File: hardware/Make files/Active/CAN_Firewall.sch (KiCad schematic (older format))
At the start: 55 parts, among them CON1 BARREL_JACK, CON2 AVR-JTAG-10, CON3 AVR-AW-6, J1 +5V_SRC, J2 DB9, J3 DB9, P1 USB_OTG, P2 USB_OTG, P3 DIAG Port, SW1 SPST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

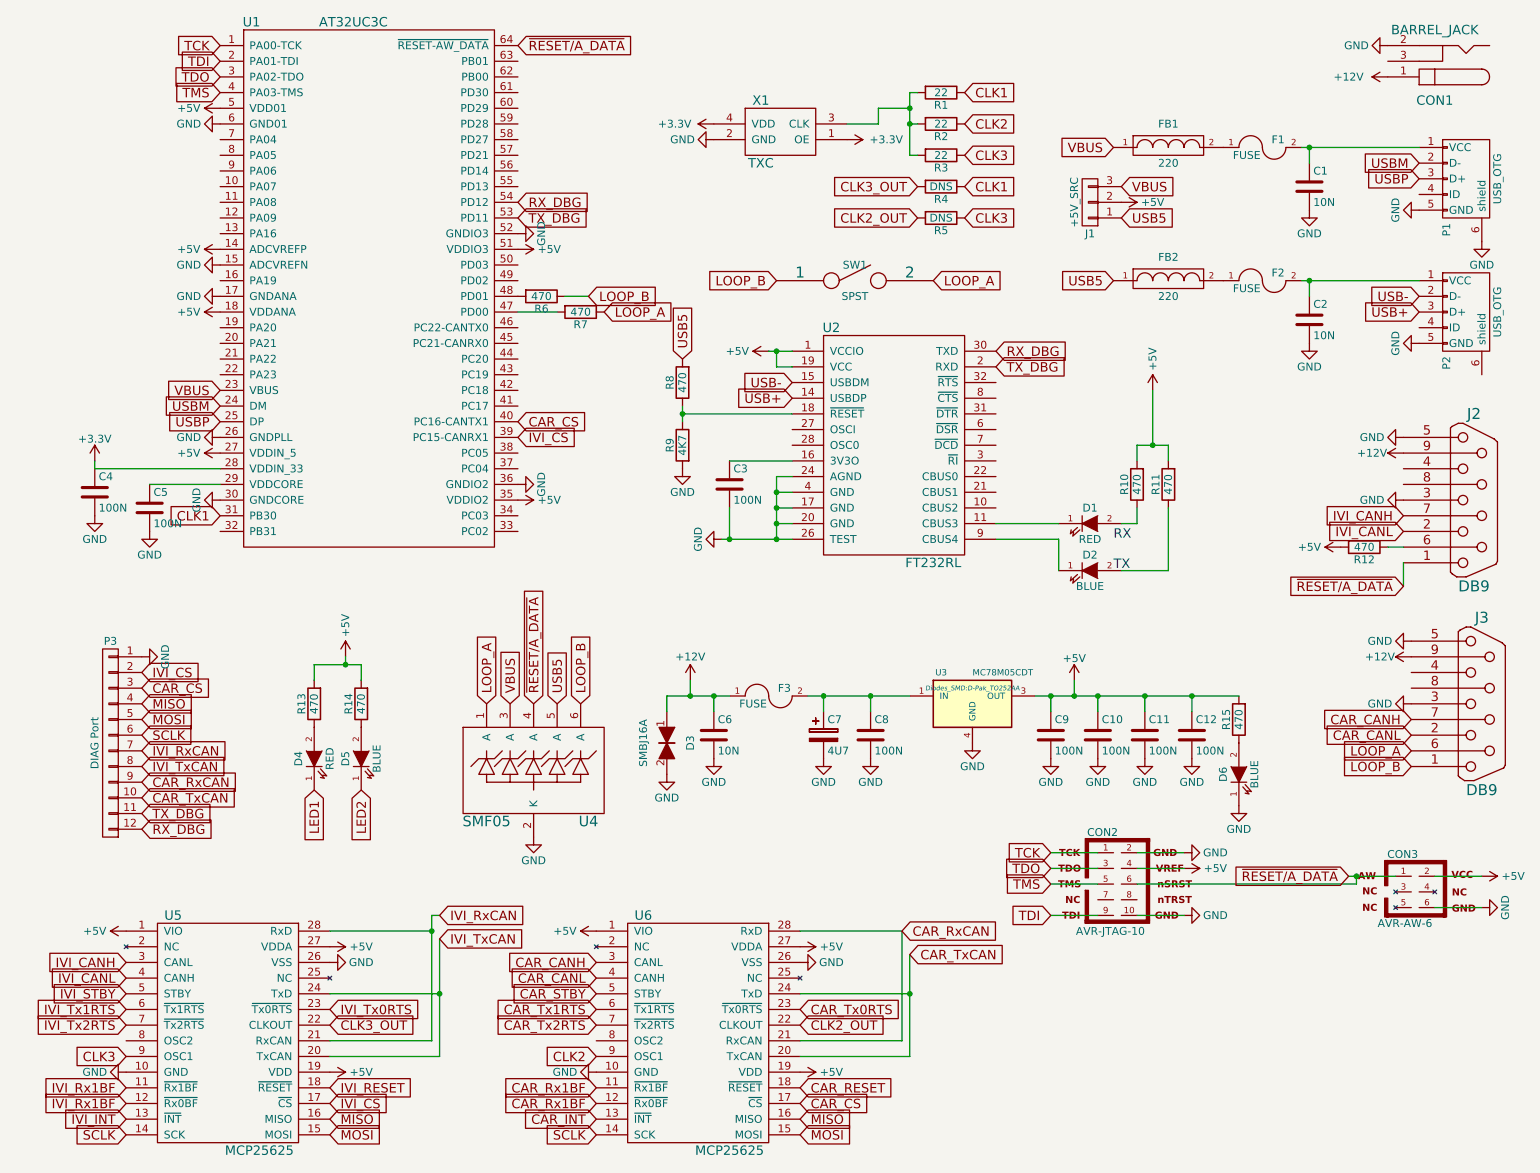
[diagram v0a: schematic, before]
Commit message: V1.1 layout pass complete
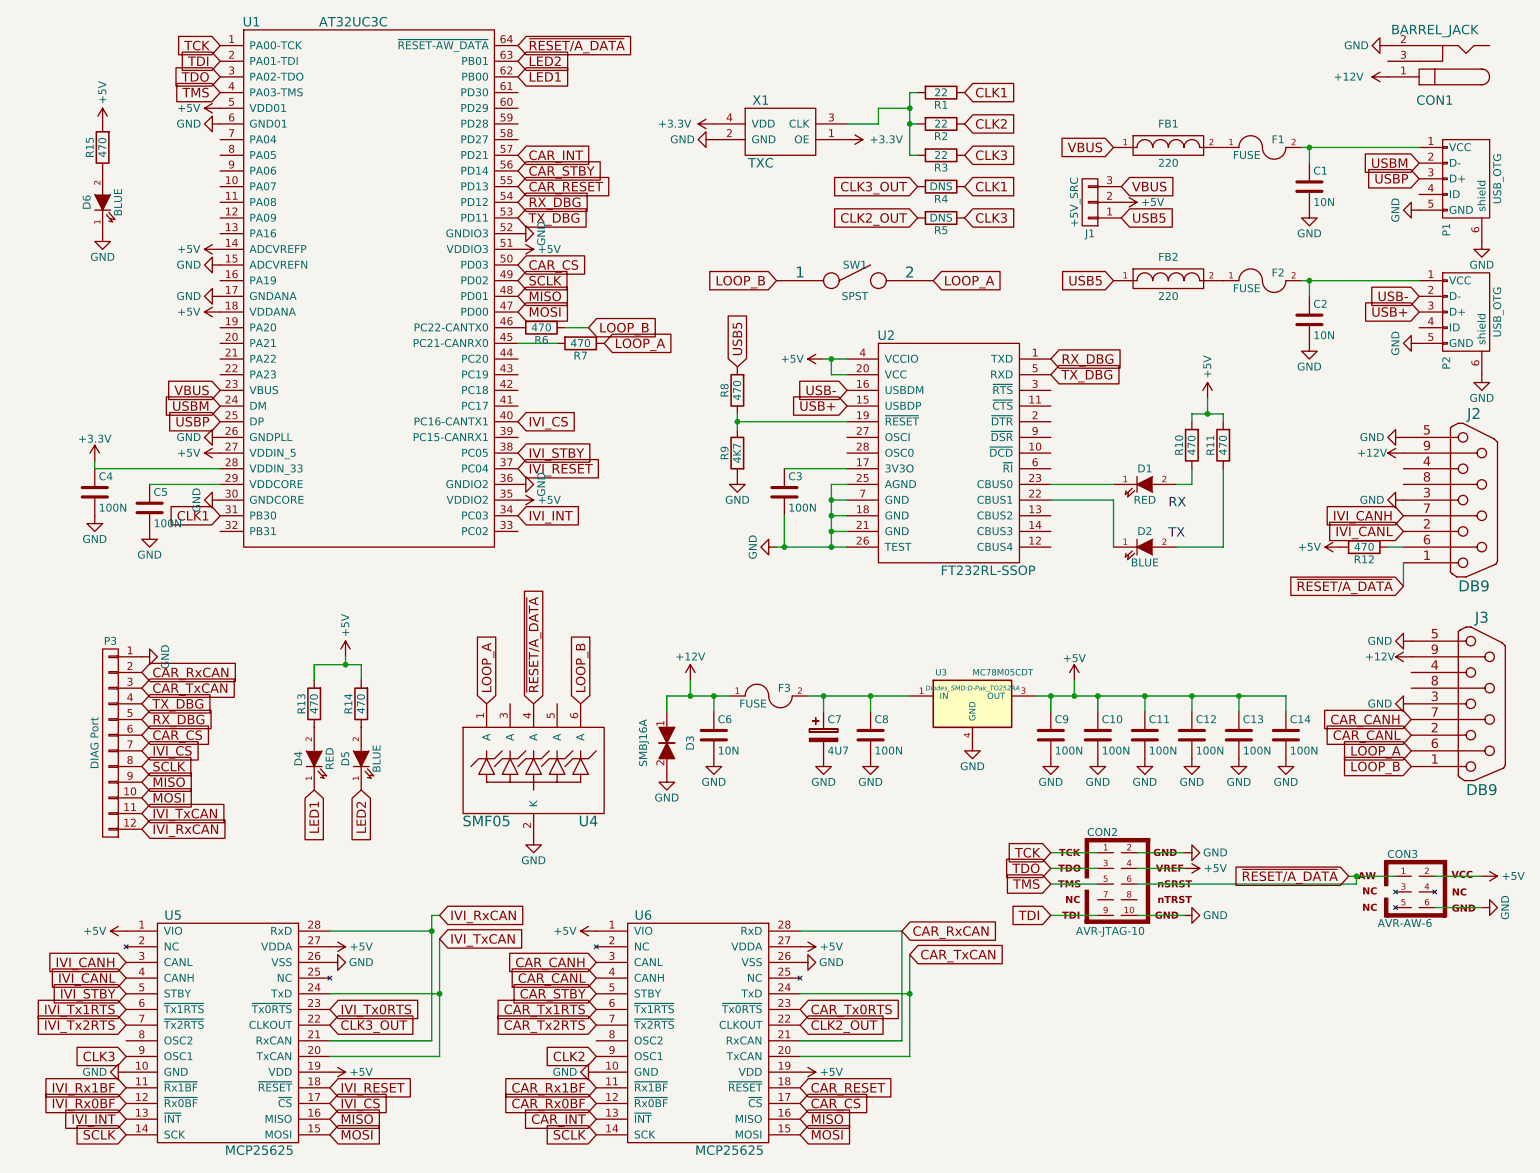
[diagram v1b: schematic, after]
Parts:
- removed U2: FT232RL, symbol FT232RL
- added C13, C14: 100N, Custom Parts:R_0603_sm, symbol C
- added U2: FT232RL-SSOP, Housings_SSOP:SSOP-28_5.3x10.2mm_Pitch0.65mm, symbol FT232RL-SSOP
- CON1: footprint (none) -> Connect:BARREL_JACK
- CON2: footprint AVR-JTAG-10 -> Socket_Strips:Socket_Strip_Straight_2x05
- CON3: footprint AVR-AW-6 -> Socket_Strips:Socket_Strip_Straight_2x03
- D1, D2, D4, D5, D6: footprint (none) -> Custom Parts:Diode_0805_12
- FB1, FB2: footprint (none) -> Custom Parts:Diode_0805_12_SM
- J1: footprint (none) -> Socket_Strips:Socket_Strip_Straight_1x03
- P1, P2: footprint (none) -> Custom Parts:USB_Micro-B-DX4R005JJ2R1800
- P3: footprint (none) -> Socket_Strips:Socket_Strip_Straight_1x12
- R1, R2, R3, R4, R5: footprint (none) -> Custom Parts:R_0603_sm
- SW1: footprint (none) -> Custom Parts:SW_SPST_FSMSM_SM
- U1: footprint (none) -> Housings_QFP:LQFP-64_10x10mm_Pitch0.5mm
- U5, U6: footprint (none) -> Housings_SSOP:SSOP-28_5.3x10.2mm_Pitch0.65mm
- X1: footprint (none) -> Custom Parts:TXC
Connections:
- net +5V: now also C13.1, C14.1, U2.20 (VCC), U2.4 (VCCIO)
- net CAR_CS: now also P3.6 (P6), U1.50 (PD03); no longer P3.3 (P3), U1.40 (PC16-CANTX1)
- net CAR_INT: now also U1.57 (PD21)
- net CAR_RESET: now also U1.55 (PD13)
- net CAR_Rx1BF: no longer U6.12 (~Rx0BF)
- net CAR_RxCAN: now also P3.2 (P2); no longer P3.9 (P9)
- net CAR_STBY: now also U1.56 (PD14)
- net CAR_TxCAN: now also P3.3 (P3); no longer P3.10 (P10)
- net GND: now also P2.6 (shield), C13.2, C14.2, U2.18 (GND), U2.21 (GND), U2.25 (AGND), U2.26 (TEST), U2.7 (GND)
- net IVI_CS: now also P3.7 (P7), U1.40 (PC16-CANTX1); no longer P3.2 (P2), U1.39 (PC15-CANRX1)
- net IVI_INT: now also U1.34 (PC03)
- net IVI_RESET: now also U1.37 (PC04)
- net IVI_Rx1BF: no longer U5.12 (~Rx0BF)
- net IVI_RxCAN: now also P3.12 (P12); no longer P3.7 (P7)
- net IVI_STBY: now also U1.38 (PC05)
- net IVI_TxCAN: now also P3.11 (P11); no longer P3.8 (P8)
- net LED1: now also U1.62 (PB00)
- net LED2: now also U1.63 (PB01)
- net MISO: now also P3.9 (P9), U1.48 (PD01); no longer P3.4 (P4)
- net MOSI: now also P3.10 (P10), U1.47 (PD00); no longer P3.5 (P5)
- net RX_DBG: now also P3.5 (P5), U2.1 (TXD); no longer P3.12 (P12)
- net SCLK: now also P3.8 (P8), U1.49 (PD02); no longer P3.6 (P6)
- net TX_DBG: now also P3.4 (P4), U2.5 (RXD); no longer P3.11 (P11)
- net USB+: now also U2.15 (USBDP)
- net USB-: now also U2.16 (USBDM)
- net USB5: no longer U4.5 (A)
- net VBUS: no longer U4.3 (A)
- net at R7.2: now also U1.45 (PC21-CANRX0); no longer U1.47 (PD00)
- net at R6.2: now also U1.46 (PC22-CANTX0); no longer U1.48 (PD01)
- net at D1.1 (K): now also U2.23 (CBUS0)
- net at C3.1: now also U2.17 (3V3O)
- net at R8.1, R9.1: now also U2.19 (~RESET)
- net at D2.1 (K): now also U2.22 (CBUS1)
- new net CAR_Rx0BF: U6.12 (~Rx0BF)
- new net IVI_Rx0BF: U5.12 (~Rx0BF)
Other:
- moved on the sheet: C3, D1, D2, D6, R10, R11, R15, R6, R7, R8, R9

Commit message: V1.11 Schematic and PCB layout
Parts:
- added R16, R17, R18, R19: 0, Custom Parts:R_0603_sm, symbol R
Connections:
- net CAR_RxCAN: now also U1.45 (PC21-CANRX0), R17.1; no longer U6.21 (RxCAN)
- net CAR_TxCAN: now also U1.46 (PC22-CANTX0), R19.1; no longer U6.20 (TxCAN)
- net IVI_CS: now also U1.41 (PC17); no longer U1.40 (PC16-CANTX1)
- net IVI_RxCAN: now also U1.39 (PC15-CANRX1), R16.1; no longer U5.21 (RxCAN)
- net IVI_TxCAN: now also U1.40 (PC16-CANTX1), R18.1; no longer U5.20 (TxCAN)
- net at R7.2: now also U1.43 (PC19); no longer U1.45 (PC21-CANRX0)
- net at R6.2: now also U1.44 (PC20); no longer U1.46 (PC22-CANTX0)
- new net: R19.2, U6.20 (TxCAN)
- new net: R17.2, U6.21 (RxCAN)
- new net: R18.2, U5.20 (TxCAN)
- new net: R16.2, U5.21 (RxCAN)
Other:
- moved on the sheet: R6, R7
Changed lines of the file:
@@
 	1    0    0    -1
 $EndComp
-Text GLabel 4150 2700 2    60   Input ~ 0
+Text GLabel 4150 2900 2    60   Input ~ 0
 LOOP_A
-Text GLabel 4050 2600 2    60   Input ~ 0
+Text GLabel 4050 2800 2    60   Input ~ 0
 LOOP_B
 $Comp
@@
 L R R7
 U 1 1 55C430A0
-P 4000 2700
-F 0 "R7" V 4080 2700 50  0000 C CNN
-F 1 "470" V 4000 2700 50  0000 C CNN
-F 2 "Custom Parts:R_0603_sm" V 3930 2700 30  0001 C CNN
-F 3 "" H 4000 2700 30  0000 C CNN
-	1    4000 2700
+P 4000 2900
+F 0 "R7" V 4080 2900 50  0000 C CNN
+F 1 "470" V 4000 2900 50  0000 C CNN
+F 2 "Custom Parts:R_0603_sm" V 3930 2900 30  0001 C CNN
+F 3 "" H 4000 2900 30  0000 C CNN
+	1    4000 2900
 	0    1    1    0
 $EndComp
@@
 L R R6
 U 1 1 55CDF193
-P 3750 2600
-F 0 "R6" V 3830 2600 50  0000 C CNN
-F 1 "470" V 3750 2600 50  0000 C CNN
-F 2 "Custom Parts:R_0603_sm" V 3680 2600 30  0001 C CNN
-F 3 "" H 3750 2600 30  0000 C CNN
-	1    3750 2600
+P 3750 2800
+F 0 "R6" V 3830 2800 50  0000 C CNN
+F 1 "470" V 3750 2800 50  0000 C CNN
+F 2 "Custom Parts:R_0603_sm" V 3680 2800 30  0001 C CNN
+F 3 "" H 3750 2800 30  0000 C CNN
+	1    3750 2800
 	0    1    1    0
 $EndComp
@@
 	6100 7250 5400 7250
 Wire Wire Line
-	6100 6600 6100 7250
-Wire Wire Line
 	6100 6850 5400 6850
 Wire Wire Line
 	5400 7150 6050 7150
-Wire Wire Line
-	6050 7150 6050 6450
 Wire Wire Line
 	6050 6450 5400 6450
@@
 	3100 7250 2400 7250
 Wire Wire Line
-	3100 6500 3100 7250
-Wire Wire Line
 	3100 6850 2400 6850
 Wire Wire Line
 	3050 7150 2400 7150
-Wire Wire Line
-	3050 6350 3050 7150
 Wire Wire Line
 	3050 6450 2400 6450
@@
 Connection ~ 7900 4950
 Wire Wire Line
-	4050 2600 3900 2600
+	4050 2800 3900 2800
 $Comp
 L SPST SW1
@@
 Text GLabel 3600 2300 2    60   Input ~ 0
 SCLK
-Text GLabel 3600 3200 2    60   Input ~ 0
+Text GLabel 3600 3100 2    60   Input ~ 0
 IVI_CS
 Wire Wire Line
-	3600 2700 3850 2700
+	3600 2900 3850 2900
 Text GLabel 3600 3400 2    60   Input ~ 0
 IVI_STBY
@@
 	8500 4950 8500 5050
 Connection ~ 8200 4950
+$Comp
+L R R16
+U 1 1 55F1D948
+P 3050 6650
+F 0 "R16" V 3130 6650 50  0000 C CNN
+F 1 "0" V 3050 6650 50  0000 C CNN
+F 2 "Custom Parts:R_0603_sm" V 2980 6650 30  0001 C CNN
+F 3 "" H 3050 6650 30  0000 C CNN
+	1    3050 6650
+	-1   0    0    -1
+$EndComp
+$Comp
+L R R18
+U 1 1 55F1E8B2
+P 3100 7050
+F 0 "R18" V 3180 7050 50  0000 C CNN
+F 1 "0" V 3100 7050 50  0000 C CNN
+F 2 "Custom Parts:R_0603_sm" V 3030 7050 30  0001 C CNN
+F 3 "" H 3100 7050 30  0000 C CNN
+	1    3100 7050
+	-1   0    0    -1
+$EndComp
+Wire Wire Line
+	3050 7150 3050 6800
+Wire Wire Line
+	3100 6500 3100 6900
+Wire Wire Line
+	3050 6350 3050 6500
+Wire Wire Line
+	3100 7200 3100 7250
+$Comp
+L R R17
+U 1 1 55F1F1AF
+P 6050 6650
+F 0 "R17" V 6130 6650 50  0000 C CNN
+F 1 "0" V 6050 6650 50  0000 C CNN
+F 2 "Custom Parts:R_0603_sm" V 5980 6650 30  0001 C CNN
+F 3 "" H 6050 6650 30  0000 C CNN
+	1    6050 6650
+	-1   0    0    -1
+$EndComp
+$Comp
+L R R19
+U 1 1 55F1F457
+P 6100 7050
+F 0 "R19" V 6180 7050 50  0000 C CNN
+F 1 "0" V 6100 7050 50  0000 C CNN
+F 2 "Custom Parts:R_0603_sm" V 6030 7050 30  0001 C CNN
+F 3 "" H 6100 7050 30  0000 C CNN
+	1    6100 7050
+	-1   0    0    -1
+$EndComp
+Wire Wire Line
+	6100 6900 6100 6600
+Wire Wire Line
+	6100 7200 6100 7250
+Wire Wire Line
+	6050 7150 6050 6800
+Wire Wire Line
+	6050 6450 6050 6500
+Text GLabel 3600 3300 2    60   Input ~ 0
+IVI_RxCAN
+Text GLabel 3600 3200 2    60   Input ~ 0
+IVI_TxCAN
+Text GLabel 3600 2700 2    60   Input ~ 0
+CAR_RxCAN
+Text GLabel 3600 2600 2    60   Input ~ 0
+CAR_TxCAN
 $EndSCHEMATC

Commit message: V1.11 Proofed
Ready to order
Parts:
- added R20, R21: 120, Custom Parts:R_0603_sm, symbol R
- added SW2, SW3: SPST, Custom Parts:SW_SPST_FSMSM_SM, symbol SPST
- D3: footprint Diodes_SMD:Diode-SMB_Standard -> Diodes_SMD:SMB_Handsoldering
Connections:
- net CAR_CANH: now also R21.2
- net CAR_CANL: now also SW3.2
- net IVI_CANH: now also R20.2
- net IVI_CANL: now also SW2.2
- net LED1: now also U1.58 (PD27); no longer U1.62 (PB00)
- net LED2: now also U1.59 (PD28); no longer U1.63 (PB01)
- new net: R20.1, SW2.1
- new net: R21.1, SW3.1
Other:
- moved on the sheet: C3, D1, D2, J1, R1, R10, R11, R2, R3, R4, R5, R8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
